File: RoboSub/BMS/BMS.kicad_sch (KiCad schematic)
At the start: 26 parts, among them J1 CAN, J2 CAN, J3 DuraClik, J4 XT90, J5 XT90, J7 ExtPwrSw, K1 A3_Relay, Q1 PMV28ENEA, SW2 DBG2, SW3 DBG1, SW4 RST, U1 VXO7803, U4 CZ3AG7_HalEfSens

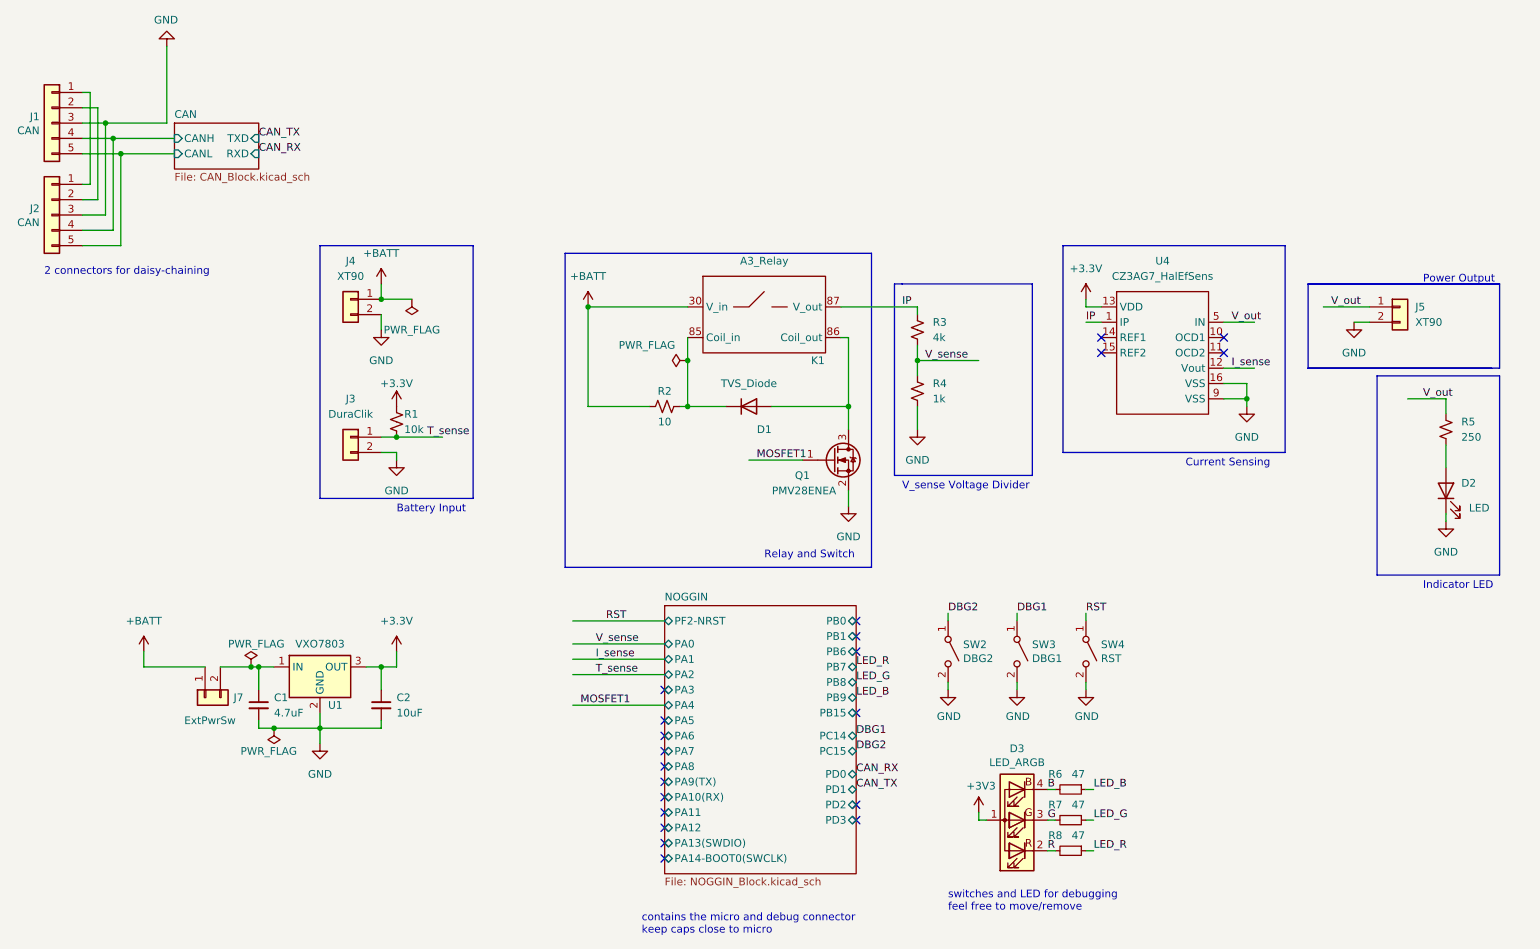
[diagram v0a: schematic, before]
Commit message: cleaned up schematic
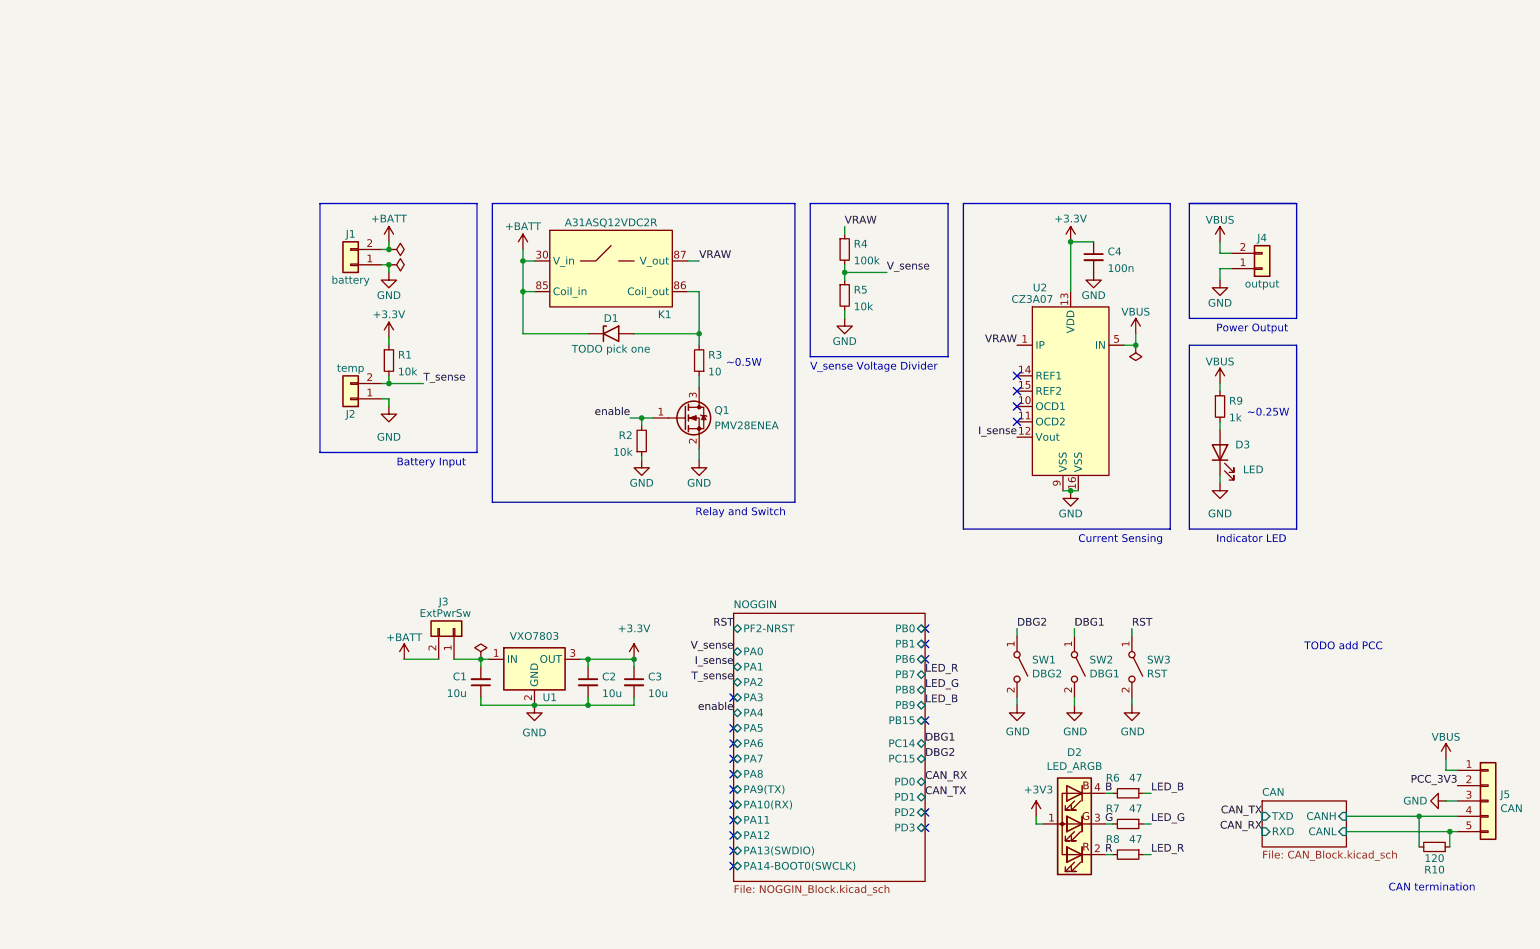
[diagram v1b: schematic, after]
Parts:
- removed D1: TVS_Diode, Diode_SMD:D_SMC, symbol Simulation_SPICE:DIODE
- removed J2: CAN, extraparts:Molex_DuraClik_Vert_5pin, symbol Connector_Generic:Conn_01x05
- removed R1: 10k, Resistor_SMD:R_0805_2012Metric, symbol Device:R_Small_US
- removed R2: 10, Resistor_SMD:R_0805_2012Metric, symbol Device:R_Small_US
- removed R3: 4k, Resistor_SMD:R_1206_3216Metric, symbol Device:R_Small_US
- removed R4: 1k, Resistor_SMD:R_0603_1608Metric, symbol Device:R_Small_US
- removed R5: 250, Resistor_SMD:R_0603_1608Metric, symbol Device:R_Small_US
- added C3: 10u, Capacitor_SMD:C_0805_2012Metric, symbol Device:C_Small
- added C4: 100n, Capacitor_SMD:C_0603_1608Metric, symbol Device:C_Small
- added D1: TODO pick one, symbol Diode:1.5KExxA
- added R1, R2, R5: 10k, Resistor_SMD:R_0603_1608Metric, symbol Device:R_Small
- added R10: 120, Resistor_SMD:R_0603_1608Metric, symbol Device:R_Small
- added R3: 10, Resistor_SMD:R_1206_3216Metric, symbol Device:R_Small
- added R4: 100k, Resistor_SMD:R_0603_1608Metric, symbol Device:R_Small
- added R9: 1k, Resistor_SMD:R_1206_3216Metric, symbol Device:R_Small
- C1: value 4.7uF -> 10u; footprint Capacitor_SMD:C_0603_1608Metric -> Capacitor_SMD:C_0805_2012Metric
- C2: value 10uF -> 10u; footprint Capacitor_SMD:C_0603_1608Metric -> Capacitor_SMD:C_0805_2012Metric
- D3: renamed from D2; footprint LED_SMD:LED_Cree-PLCC4_2x2mm_CW -> LED_SMD:LED_0603_1608Metric
- J1: renamed from J4; value XT90 -> battery
- J2: renamed from J3; value DuraClik -> temp
- J4: renamed from J5; value XT90 -> output
- K1: value A3_Relay -> A31ASQ12VDC2R
- U2: renamed from U4; value CZ3AG7_HalEfSens -> CZ3A07
- renumbered D3 to D2, J7 to J3, J1 to J5, SW2 to SW1, SW3 to SW2, SW4 to SW3
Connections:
- net +3V3: now also C3.1, C4.1, R1.1
- net +BATT: now also J1.2 (Pin_2), J3.2 (Pin_2), K1.85 (Coil_in), D1.1 (A1); no longer J1.1 (Pin_1), J3.1 (Pin_1)
- net CAN/CANH: now also R10.2
- net CAN/CANL: now also R10.1
- net GND: now also C1.1, J1.1 (Pin_1), J2.1 (Pin_1), J4.1 (Pin_1), C3.2, C4.2, R2.1, R5.2; no longer C1.2, J1.2 (Pin_2), J2.2 (Pin_2), J4.2 (Pin_2)
- net T_sense: now also J2.2 (Pin_2), R1.2; no longer J2.1 (Pin_1)
- net V_sense: now also R4.2, R5.1
- net VBUS: now reaches J5.1 (Pin_1)
- net VBUS: now also J4.2 (Pin_2), U2.5 (IN), R9.1
- net PCC_3V3: now reaches J5.2 (Pin_2)
- net at K1.86 (Coil_out): now also D1.2 (A2), R3.2; no longer Q1.3 (D)
- net at D3.2 (A): now also R9.2
- net IP renamed VRAW
- net VRAW: now also R4.1
- net MOSFET1 renamed enable
- net enable: now also R2.2
- removed net V_out: J4.1 (Pin_1), U2.5 (IN)
- new net: C1.2, J3.1 (Pin_1), U1.1 (IN)
- new net: Q1.3 (D), R3.1
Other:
- note added: "CAN termination"
- note added: "TODO add PCC"
- note added: "~0.25W"
- note added: "~0.5W"
- note removed: "2 connectors for daisy-chaining"
- note removed: "contains the micro and debug connector keep caps close to micro"
- note removed: "switches and LED for debugging feel free to move/remove"
- moved on the sheet: D2, D3, J1, J2, J3, J4, J5, Q1, R6, R7, R8, SW1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

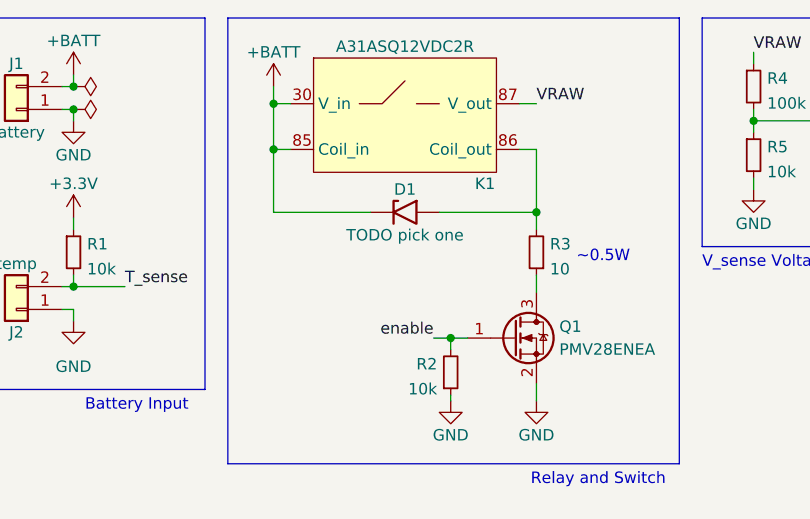
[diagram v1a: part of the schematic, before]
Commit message: added model num for TVS diode
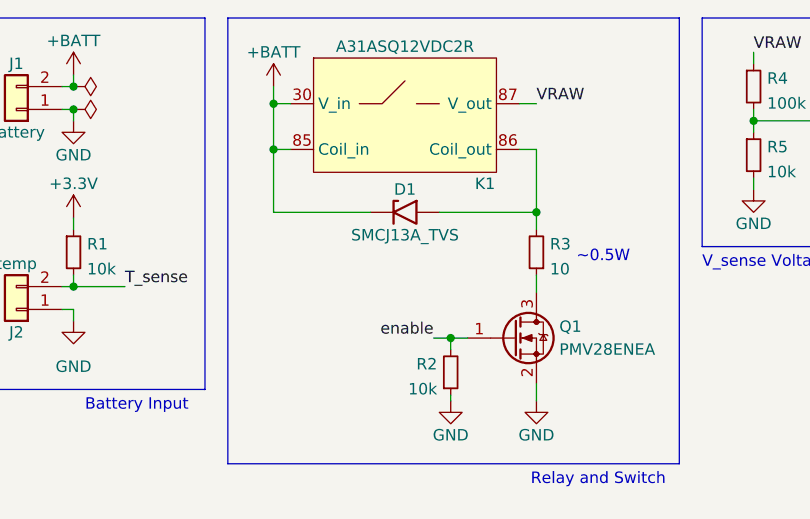
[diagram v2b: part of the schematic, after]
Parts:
- D1: value TODO pick one -> SMCJ13A_TVS
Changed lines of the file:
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@@
     (in_bom yes) (on_board yes)
     (property "Reference" "D1" (id 0) (at 113.03 65.405 0))
-    (property "Value" "TODO pick one" (id 1) (at 113.03 70.485 0))
+    (property "Value" "SMCJ13A_TVS" (id 1) (at 113.03 70.485 0))
     (property "Footprint" "" (id 2) (at 113.03 73.025 0)
       (effects (font (size 1.27 1.27)) hide)
@@
     )
     (path "/4a45b954-d385-430f-a2ee-394c29269c8b"
-      (reference "D1") (unit 1) (value "TODO pick one") (footprint "")
+      (reference "D1") (unit 1) (value "SMCJ13A_TVS") (footprint "")
     )
     (path "/00000000-0000-0000-0000-00005e635a64"

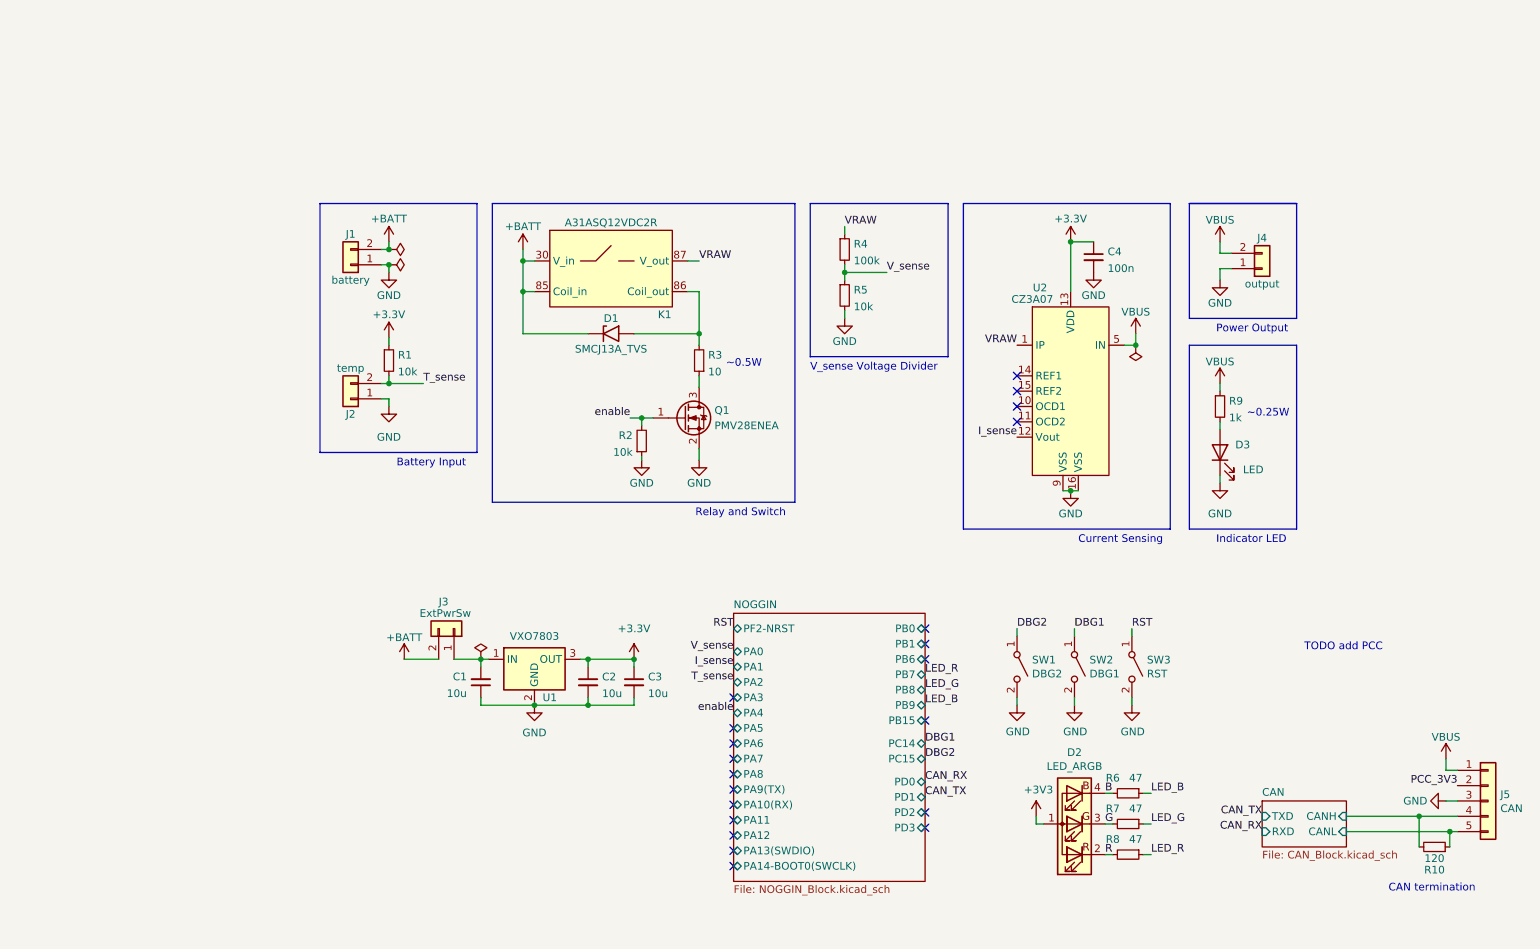
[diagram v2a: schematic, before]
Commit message: Added PCC to schematic
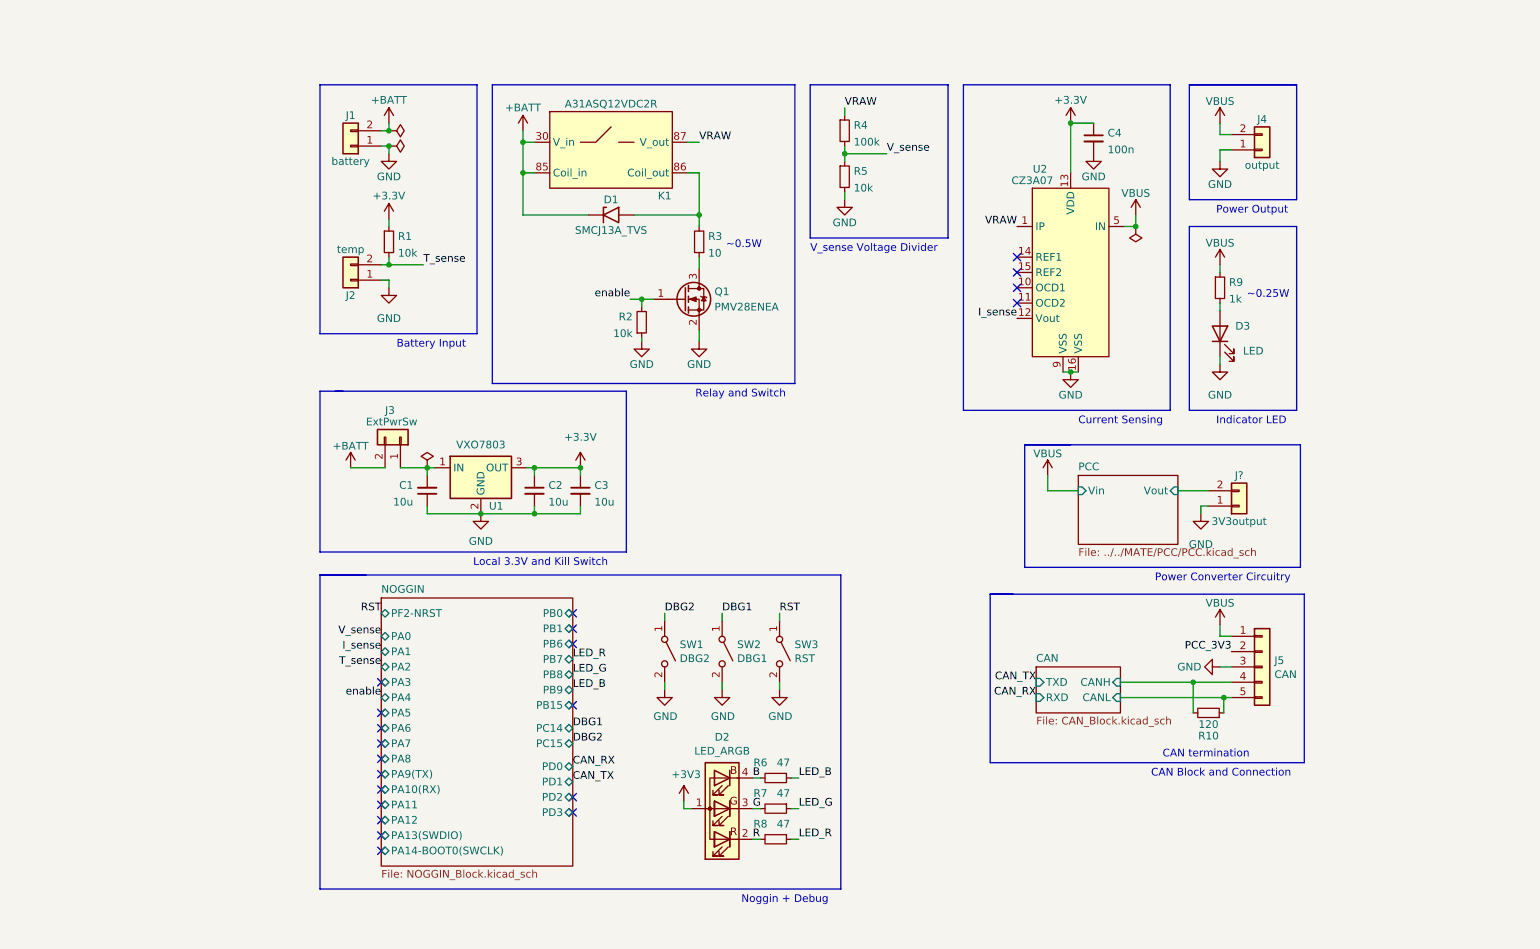
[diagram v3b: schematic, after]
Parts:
- added J?: 3V3output, BMS_Library:Conn_XT90, symbol Connector_Generic:Conn_01x02
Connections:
- net GND: now also J?.1 (Pin_1)
- new net PCC/Vout: J?.2 (Pin_2)
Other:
- added sheet PCC (../../MATE/PCC/PCC.kicad_sch)
- note added: "CAN Block and Connection"
- note added: "Local 3.3V and Kill Switch"
- note added: "Noggin + Debug"
- note added: "Power Converter Circuitry"
- note removed: "TODO add PCC"
- moved on the sheet: C1, C2, C3, C4, D1, D2, D3, J1, J2, J3, J4, J5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

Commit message: incorporating PCC into BMS
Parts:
- removed J?: 3V3output, BMS_Library:Conn_XT90, symbol Connector_Generic:Conn_01x02
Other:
- removed sheet PCC
- note added: "TODO: Custom Symbol + Footprint for PCC"
